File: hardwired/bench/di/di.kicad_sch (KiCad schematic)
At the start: 14 parts, among them U1 ${SIM.PARAMS}, U2 ${SIM.PARAMS}

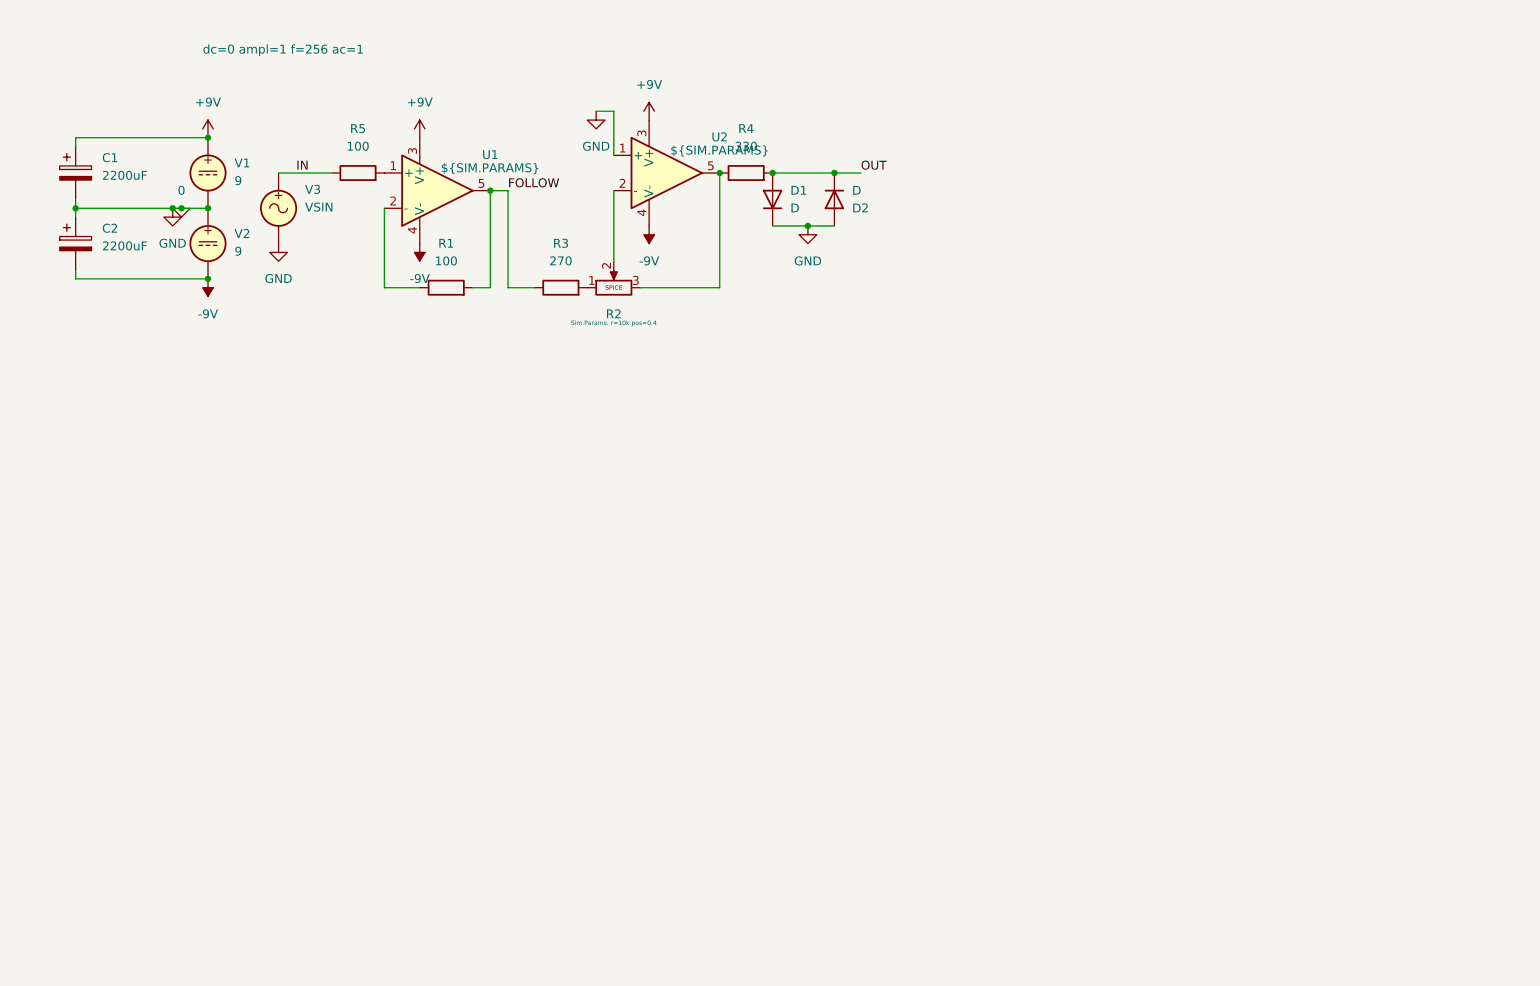
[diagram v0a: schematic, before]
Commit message: Add some layout for DI box
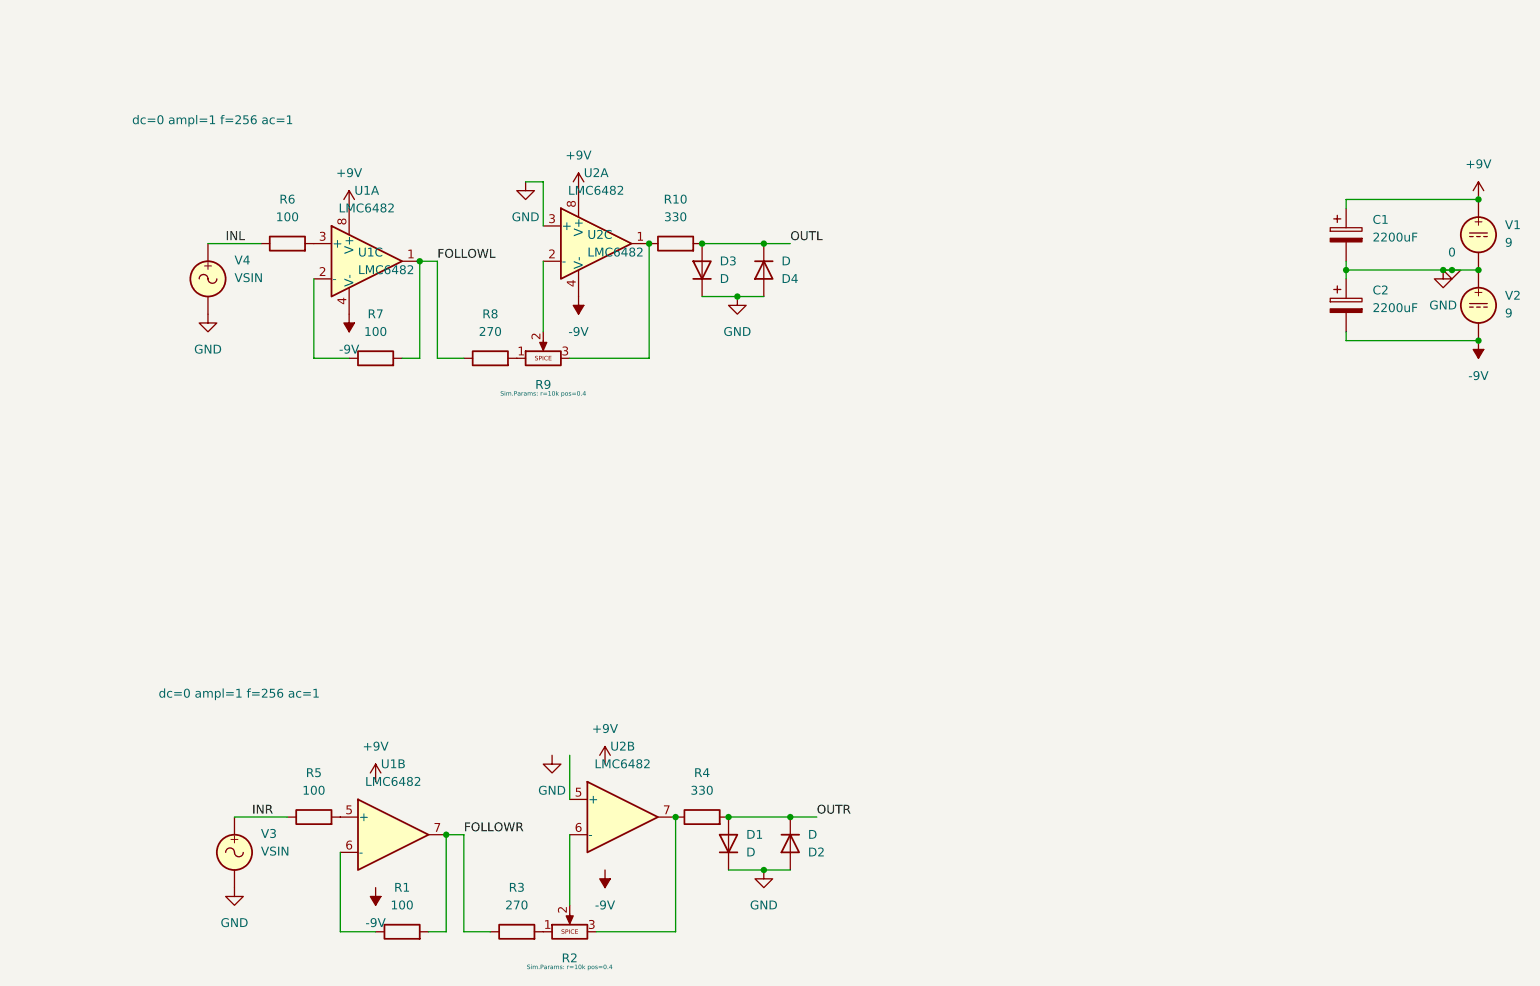
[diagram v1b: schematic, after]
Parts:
- removed U1, U2: ${SIM.PARAMS}, symbol Simulation_SPICE:OPAMP
- added D3, D4: D, Diode_THT:D_A-405_P10.16mm_Horizontal, symbol Device:D
- added R10: 330, Resistor_THT:R_Axial_DIN0207_L6.3mm_D2.5mm_P10.16mm_Horizontal, symbol Device:R
- added R6, R7: 100, Resistor_THT:R_Axial_DIN0207_L6.3mm_D2.5mm_P10.16mm_Horizontal, symbol Device:R
- added R8: 270, Resistor_THT:R_Axial_DIN0207_L6.3mm_D2.5mm_P10.16mm_Horizontal, symbol Device:R
- added R9: Potentiometer, Connector_PinHeader_2.54mm:PinHeader_1x02_P2.54mm_Vertical_SMD_Pin1Right, symbol Simulation_SPICE:Potentiometer
- added U1, U2: LMC6482, Package_DIP:DIP-8_W7.62mm, symbol Amplifier_Operational:LMC6482
- added V4: VSIN, symbol Simulation_SPICE:VSIN
- D1, D2: footprint (none) -> Diode_THT:D_A-405_P10.16mm_Horizontal
- R1, R3, R4, R5: footprint (none) -> Resistor_THT:R_Axial_DIN0207_L6.3mm_D2.5mm_P10.16mm_Horizontal
- R2: footprint (none) -> Connector_PinHeader_2.54mm:PinHeader_1x02_P2.54mm_Vertical_SMD_Pin1Right
- V1, V2: footprint (none) -> Connector_PinHeader_2.54mm:PinHeader_1x01_P2.54mm_Vertical
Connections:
- net +9V: now also U1.8 (V+), U2.8 (V+)
- net -9V: now also U1.4 (V-), U2.4 (V-)
- net 0: now also D3.1 (K), D4.2 (A), U2.3 (+), V4.2
- net at R1.1: now also U1.6 (-)
- net at R2.2: now also U2.6 (-)
- net at R2.3, R4.1: now also U2.7
- net at R5.2: now also U1.5 (+)
- net FOLLOW renamed FOLLOWR
- net FOLLOWR: now also U1.7
- net IN renamed INR
- net OUT renamed OUTR
- new net: R10.1, R9.3, U2.1
- new net: R6.2, U1.3 (+)
- new net: R7.1, U1.2 (-)
- new net: R9.2, U2.2 (-)
- new net: R8.2, R9.1
- new net FOLLOWL: R7.2, R8.1, U1.1
- new net INL: R6.1, V4.1
- new net OUTL: D3.2 (A), D4.1 (K), R10.2
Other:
- company: (none) -> Hardwired Design
- title: (none) -> Active Signal Probe Interface
- moved on the sheet: C1, C2, D1, D2, R1, R2, R3, R4, R5, V1, V2, V3

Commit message: DI (Signal Tracer) circuit improvements
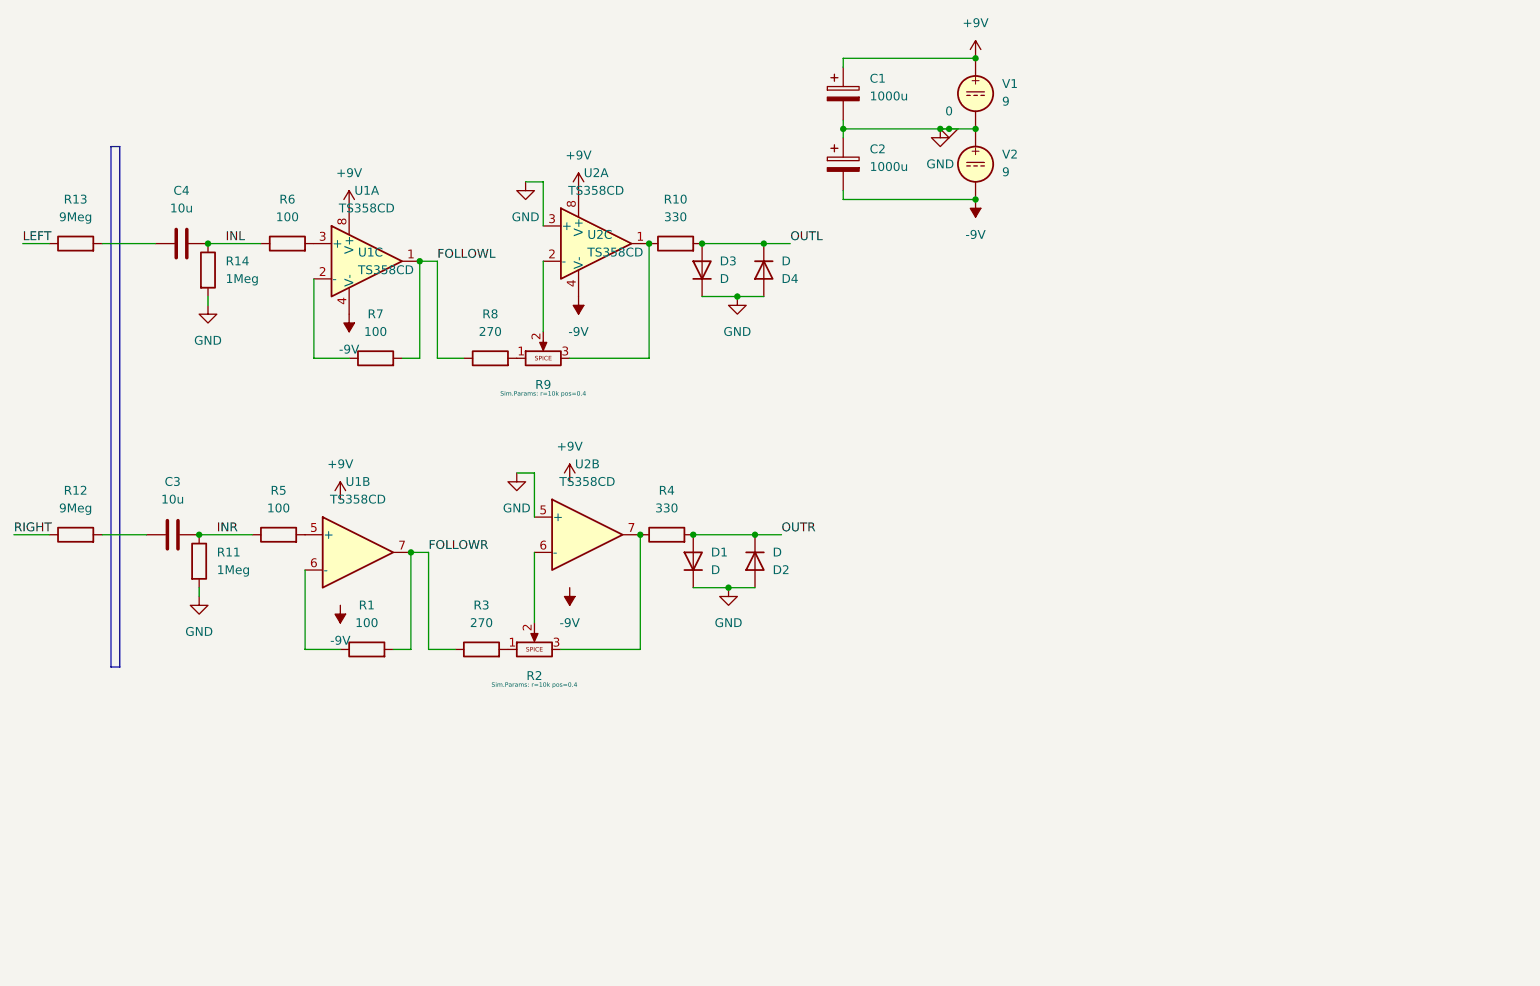
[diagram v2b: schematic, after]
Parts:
- removed V3, V4: VSIN, symbol Simulation_SPICE:VSIN
- added C3, C4: 10u, symbol Device:C
- added R11, R14: 1Meg, symbol Device:R
- added R12, R13: 9Meg, symbol Device:R
- C1, C2: value 2200uF -> 1000u
- R1, R10, R3, R4, R5, R7: footprint Resistor_THT:R_Axial_DIN0207_L6.3mm_D2.5mm_P10.16mm_Horizontal -> Resistor_THT:R_Axial_DIN0204_L3.6mm_D1.6mm_P2.54mm_Vertical
- R2, R9: footprint Connector_PinHeader_2.54mm:PinHeader_1x02_P2.54mm_Vertical_SMD_Pin1Right -> Connector_PinHeader_2.54mm:PinHeader_1x03_P2.54mm_Vertical
- U1, U2: value LMC6482 -> TS358CD
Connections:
- net 0: now also U2.5 (+), R11.2, R14.2
- net INL: now also C4.2, R14.1
- net INR: now also C3.2, R11.1
- new net: C3.1, R12.2
- new net: C4.1, R13.2
- new net LEFT: R13.1
- new net RIGHT: R12.1
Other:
- moved on the sheet: C1, C2, D1, D2, R1, R2, R3, R4, R5, U1B, U2B, V1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
